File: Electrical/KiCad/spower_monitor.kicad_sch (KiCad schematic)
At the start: 45 parts, among them J28 5V to 6V Connect, J3 5V Connect, J4 Terminal Block, J5 6V Connect, Q1 CSD17304Q3, Q2 CSD17304Q3, Q3 CSD13202Q2, U1 TLVM13640RDLR, U2 TPS40305DRCR

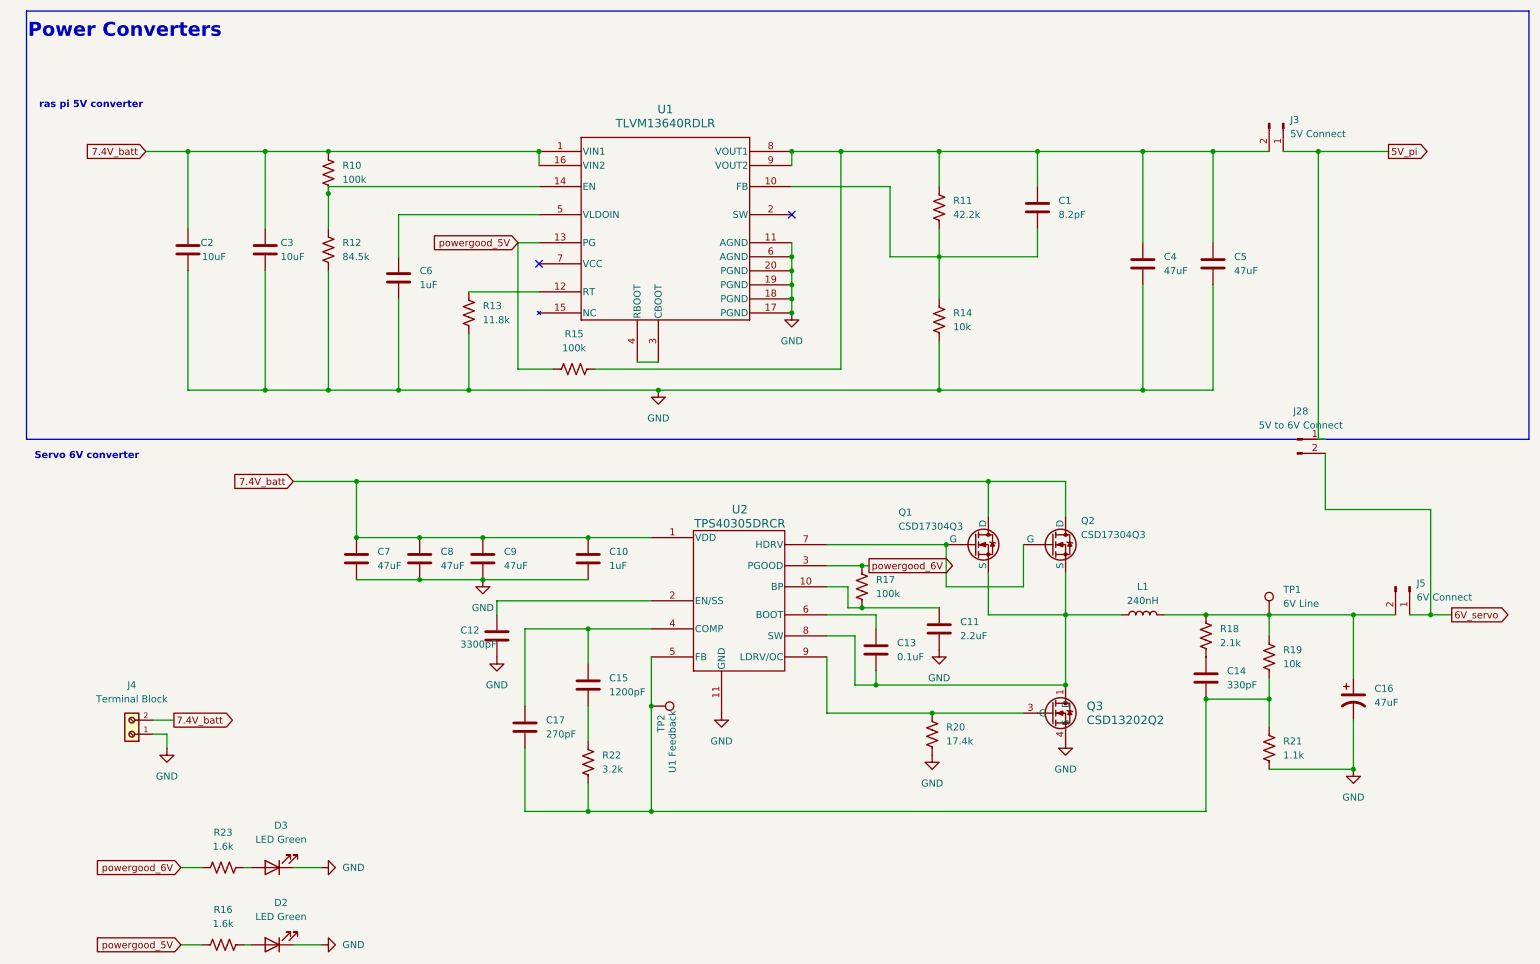
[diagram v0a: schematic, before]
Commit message: Finished Rev2 of the PCB
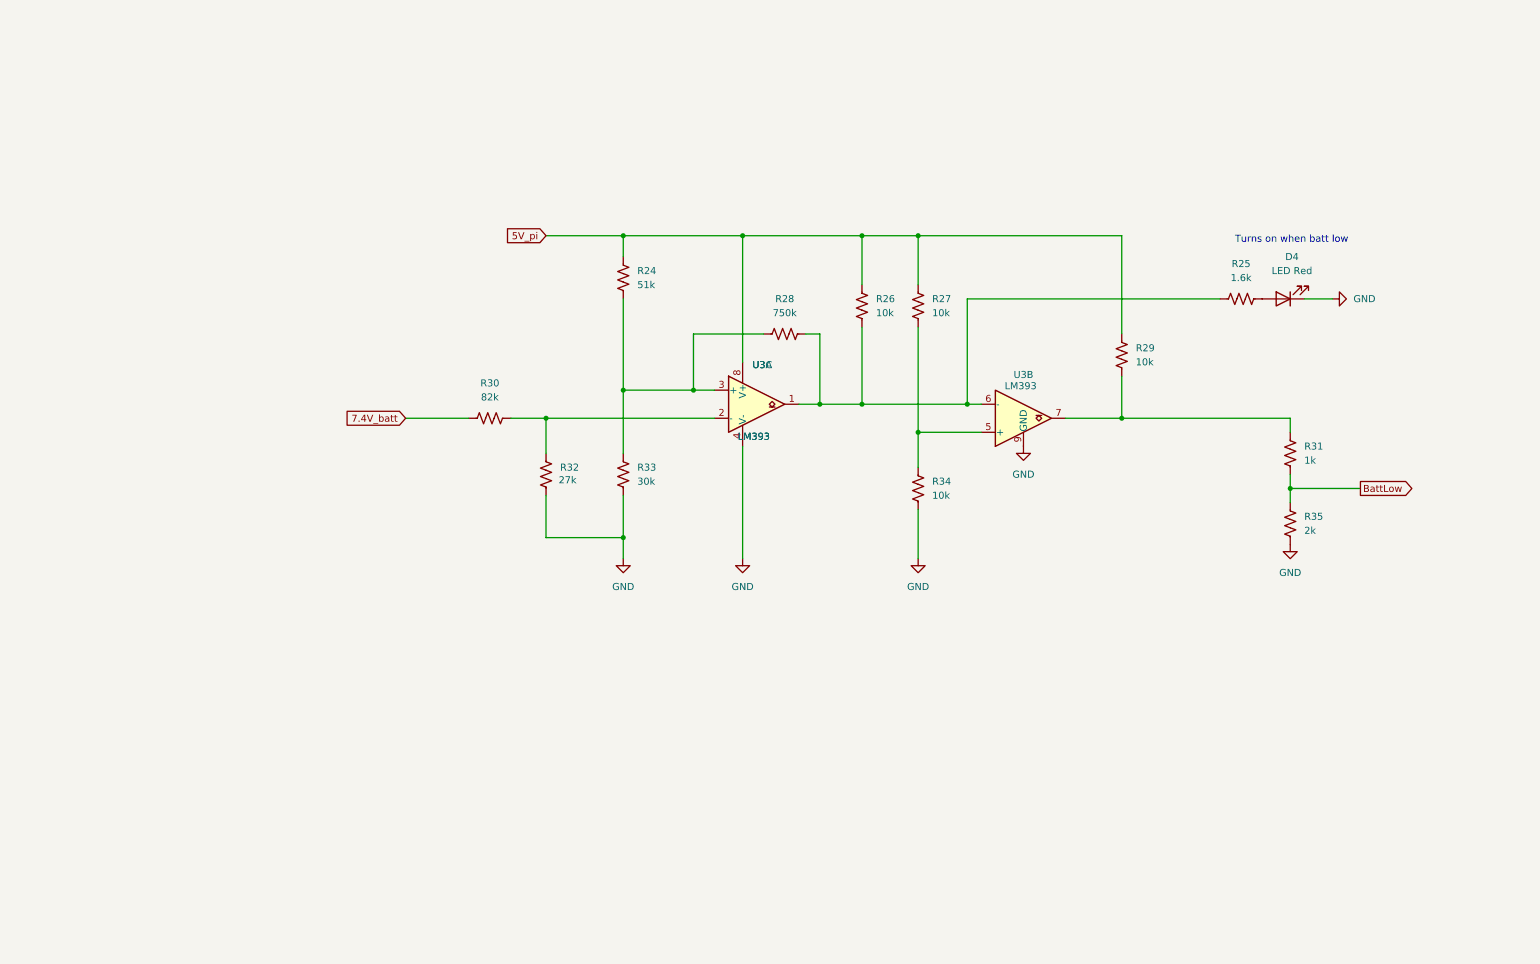
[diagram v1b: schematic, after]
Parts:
- removed C1: 8.2pF, Capacitor_SMD:C_0603_1608Metric_Pad1.08x0.95mm_HandSolder, symbol Device:C
- removed C10: 1uF, Capacitor_SMD:C_0805_2012Metric_Pad1.18x1.45mm_HandSolder, symbol Device:C
- removed C11: 2.2uF, Capacitor_SMD:C_0805_2012Metric_Pad1.18x1.45mm_HandSolder, symbol Device:C
- removed C12: 3300pF, Capacitor_SMD:C_0603_1608Metric_Pad1.08x0.95mm_HandSolder, symbol Device:C
- removed C13: 0.1uF, Capacitor_SMD:C_0603_1608Metric_Pad1.08x0.95mm_HandSolder, symbol Device:C
- removed C14: 330pF, Capacitor_SMD:C_0603_1608Metric_Pad1.08x0.95mm_HandSolder, symbol Device:C
- removed C15: 1200pF, Capacitor_SMD:C_0805_2012Metric_Pad1.18x1.45mm_HandSolder, symbol Device:C
- removed C16: 47uF, Spiderbot:PCAP_TPE_B2_PAN_1411, symbol Device:C_Polarized_US
- removed C17: 270pF, Capacitor_SMD:C_0603_1608Metric_Pad1.08x0.95mm_HandSolder, symbol Device:C
- removed C2, C3: 10uF, Capacitor_SMD:C_1210_3225Metric_Pad1.33x2.70mm_HandSolder, symbol Device:C
- removed C4, C5, C7, C8, C9: 47uF, Capacitor_SMD:C_1210_3225Metric_Pad1.33x2.70mm_HandSolder, symbol Device:C
- removed C6: 1uF, Capacitor_SMD:C_0603_1608Metric_Pad1.08x0.95mm_HandSolder, symbol Device:C
- removed D2, D3: LED Green, LED_SMD:LED_0603_1608Metric_Pad1.05x0.95mm_HandSolder, symbol Device:LED
- removed J28: 5V to 6V Connect, Connector_PinSocket_2.54mm:PinSocket_1x02_P2.54mm_Vertical, symbol Connector:Conn_01x02_Pin
- removed J3: 5V Connect, Connector_PinSocket_2.54mm:PinSocket_1x02_P2.54mm_Vertical, symbol Connector:Conn_01x02_Pin
- removed J4: Terminal Block, TerminalBlock_MetzConnect:TerminalBlock_MetzConnect_Type011_RT05502HBWC_1x02_P5.00mm_Horizontal, symbol Alecs_Lib:Terminal
- removed J5: 6V Connect, Connector_PinSocket_2.54mm:PinSocket_1x02_P2.54mm_Vertical, symbol Connector:Conn_01x02_Pin
- removed L1: 240nH, Spiderbot:IND_IHLP-4040DZ_VIS, symbol Device:L
- removed Q1, Q2: CSD17304Q3, Spiderbot:8VSON, symbol Simulation_SPICE:NMOS
- removed Q3: CSD13202Q2, Spiderbot:Q2_SON6_TEX, symbol Alecs_Lib:CSD13202Q2
- removed R10, R15, R17: 100k, Resistor_SMD:R_0603_1608Metric_Pad0.98x0.95mm_HandSolder, symbol Device:R_US
- removed R11: 42.2k, Resistor_SMD:R_0603_1608Metric_Pad0.98x0.95mm_HandSolder, symbol Device:R_US
- removed R12: 84.5k, Resistor_SMD:R_0402_1005Metric_Pad0.72x0.64mm_HandSolder, symbol Device:R_US
- removed R13: 11.8k, Resistor_SMD:R_0603_1608Metric_Pad0.98x0.95mm_HandSolder, symbol Device:R_US
- removed R14, R19: 10k, Resistor_SMD:R_0603_1608Metric_Pad0.98x0.95mm_HandSolder, symbol Device:R_US
- removed R16, R23: 1.6k, Resistor_SMD:R_0603_1608Metric_Pad0.98x0.95mm_HandSolder, symbol Device:R_US
- removed R18: 2.1k, Resistor_SMD:R_0603_1608Metric_Pad0.98x0.95mm_HandSolder, symbol Device:R_US
- removed R20: 17.4k, Resistor_SMD:R_0402_1005Metric_Pad0.72x0.64mm_HandSolder, symbol Device:R_US
- removed R21: 1.1k, Resistor_SMD:R_0603_1608Metric_Pad0.98x0.95mm_HandSolder, symbol Device:R_US
- removed R22: 3.2k, Capacitor_SMD:C_0805_2012Metric_Pad1.18x1.45mm_HandSolder, symbol Device:R_US
- removed TP1: 6V Line, TestPoint:TestPoint_Loop_D1.80mm_Drill1.0mm_Beaded, symbol Connector:TestPoint
- removed TP2: U1 Feedback, TestPoint:TestPoint_Loop_D1.80mm_Drill1.0mm_Beaded, symbol Connector:TestPoint
- removed U1: TLVM13640RDLR, Spiderbot:B3QFN20_RDL_TEX, symbol Alecs_Lib:TLVM13640RDLR
- removed U2: TPS40305DRCR, Package_SON:VSON-10-1EP_3x3mm_P0.5mm_EP1.2x2mm_ThermalVias, symbol Alecs_Lib:TPS40305DRCR
- added D4: LED Red, LED_SMD:LED_0603_1608Metric_Pad1.05x0.95mm_HandSolder, symbol Device:LED
- added R24: 51k, Resistor_SMD:R_0603_1608Metric_Pad0.98x0.95mm_HandSolder, symbol Device:R_US
- added R25: 1.6k, Resistor_SMD:R_0603_1608Metric_Pad0.98x0.95mm_HandSolder, symbol Device:R_US
- added R26, R27, R29, R34: 10k, Resistor_SMD:R_0603_1608Metric_Pad0.98x0.95mm_HandSolder, symbol Device:R_US
- added R28: 750k, Resistor_SMD:R_0603_1608Metric_Pad0.98x0.95mm_HandSolder, symbol Device:R_US
- added R30: 82k, Resistor_SMD:R_0603_1608Metric_Pad0.98x0.95mm_HandSolder, symbol Device:R_US
- added R31: 1k, Resistor_SMD:R_0603_1608Metric_Pad0.98x0.95mm_HandSolder, symbol Device:R_US
- added R32: 27k, Resistor_SMD:R_0603_1608Metric_Pad0.98x0.95mm_HandSolder, symbol Device:R_US
- added R33: 30k, Resistor_SMD:R_0603_1608Metric_Pad0.98x0.95mm_HandSolder, symbol Device:R_US
- added R35: 2k, Resistor_SMD:R_0603_1608Metric_Pad0.98x0.95mm_HandSolder, symbol Device:R_US
- added U3: LM393, Package_SO:SOIC-8-1EP_3.9x4.9mm_P1.27mm_EP2.29x3mm, symbol Comparator:LM393
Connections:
- net 5V_pi: now also R24.1, R26.1, R27.1, R29.1, U3.8 (V+)
- net 7.4V_batt: now also R30.1
- net GND: now also D4.1 (K), R32.2, R33.2, R34.2, R35.1, U3.4 (V-), U3.9 (GND)
- new net: R27.2, R34.1, U3.5 (+)
- new net: R25.1, R26.2, R28.2, U3.1, U3.6 (-)
- new net: R29.2, R31.1, U3.7
- new net: R30.2, R32.1, U3.2 (-)
- new net: D4.2 (A), R25.2
- new net: R24.2, R28.1, R33.1, U3.3 (+)
- new net BattLow: R31.2, R35.2
- no-connect marks 2 -> 0
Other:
- note added: "Turns on when batt low"
- note removed: "Power Converters"
- note removed: "Servo 6V converter"
- note removed: "ras pi 5V converter"

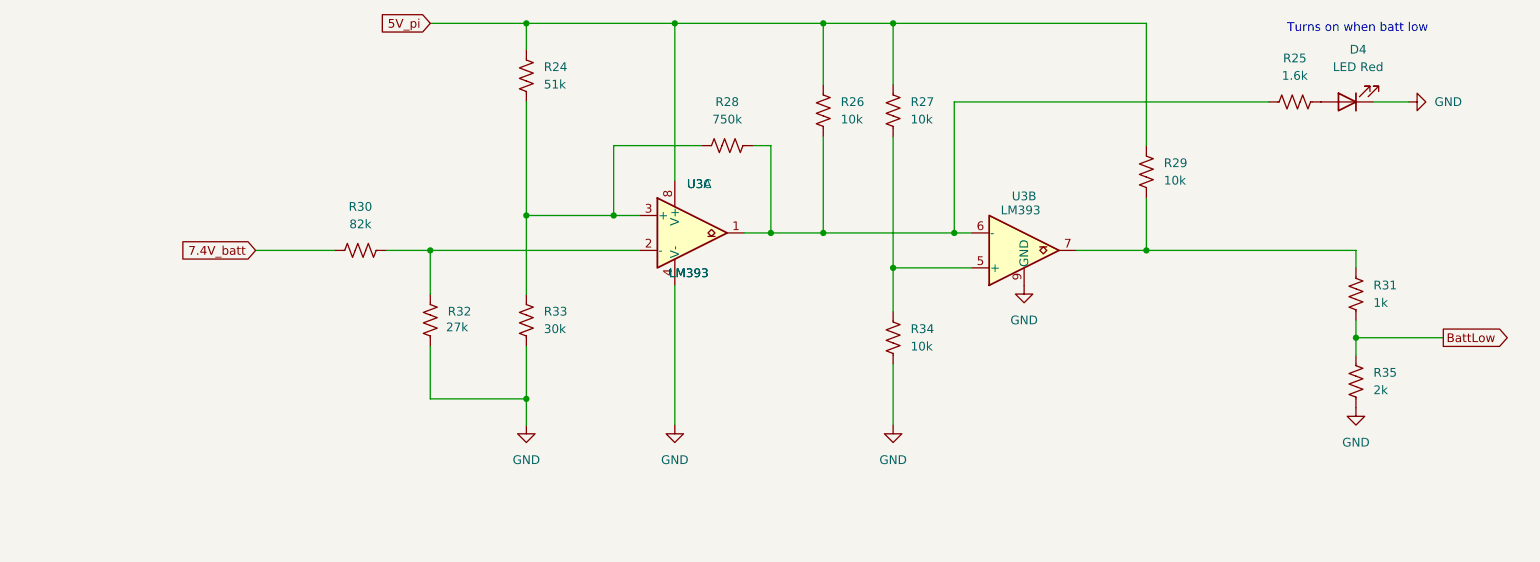
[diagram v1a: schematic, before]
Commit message: Added some labels to the schematic
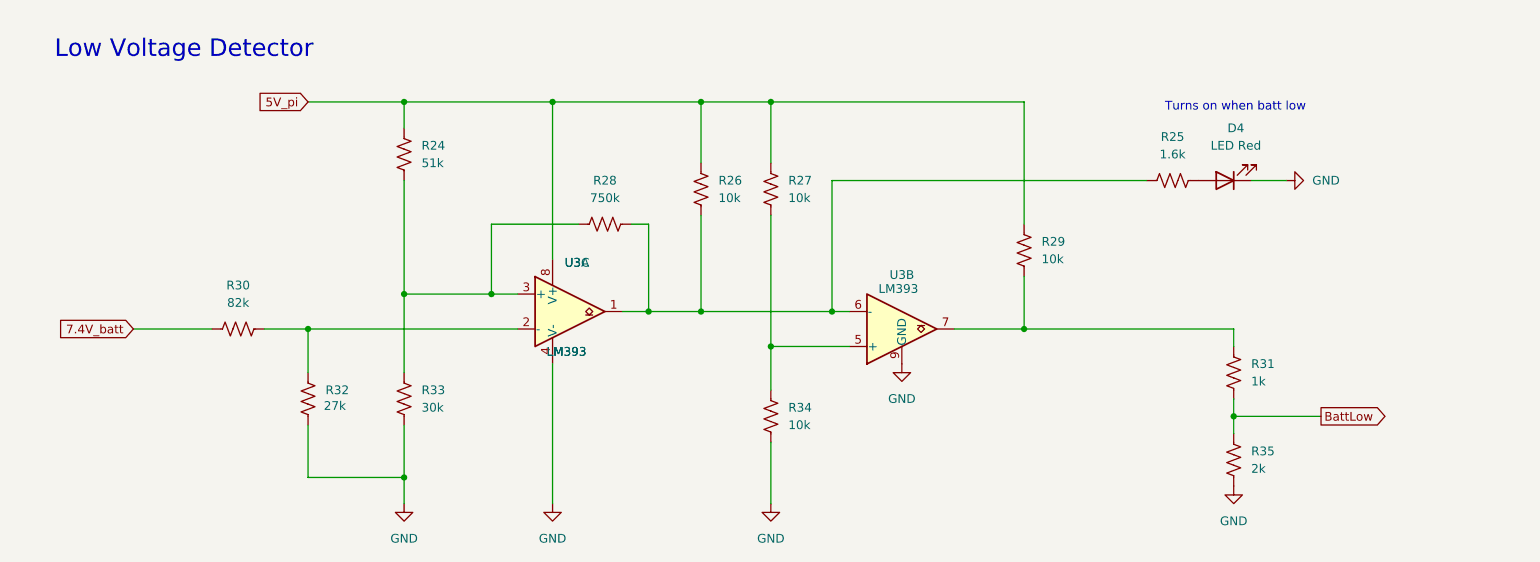
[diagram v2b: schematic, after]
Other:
- note added: "Low Voltage Detector"
- moved on the sheet: D4, R24, R25, R26, R27, R28, R29, R30, R31, R32, R33, R34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
